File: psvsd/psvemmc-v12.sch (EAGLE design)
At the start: 36 parts, among them U1 USB2244QFN, U2 LP3996_DSC_10, U3 TXS02612, X1 ZX62D-B-5PA8, Y1 XRCGB

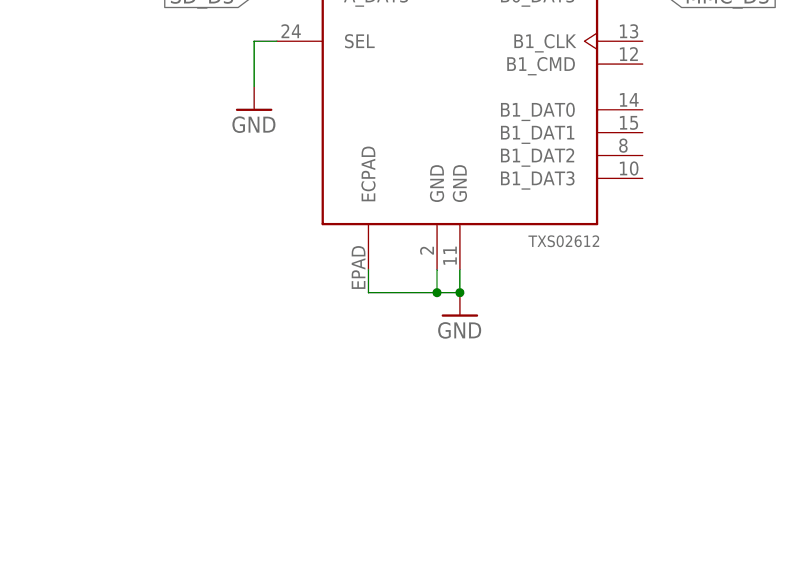
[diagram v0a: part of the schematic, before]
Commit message: psvemmc v1.2: unified drill sizes, added thermal vias to TTL translation IC
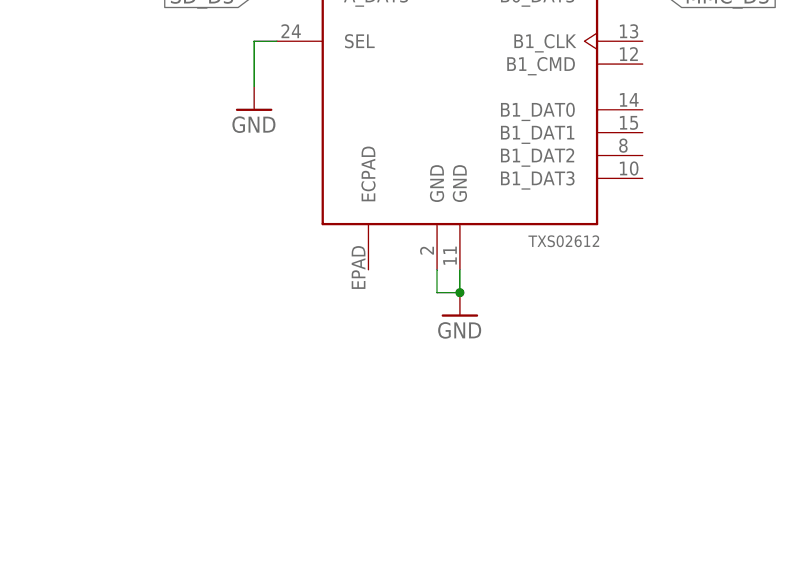
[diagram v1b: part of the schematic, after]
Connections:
- net GND: no longer U3.ECPAD
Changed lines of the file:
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@@
 <pinref part="GND18" gate="1" pin="GND"/>
 <junction x="200.66" y="43.18"/>
-<pinref part="U3" gate="G$1" pin="ECPAD"/>
-<wire x1="190.5" y1="45.72" x2="190.5" y2="43.18" width="0.1524" layer="91"/>
-<wire x1="190.5" y1="43.18" x2="198.12" y2="43.18" width="0.1524" layer="91"/>
-<junction x="198.12" y="43.18"/>
 </segment>
 </net>
